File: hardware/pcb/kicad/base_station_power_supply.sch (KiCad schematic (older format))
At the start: 18 parts, among them CON1 POWER_JACK_TART, IC1 BRIDGE_TART

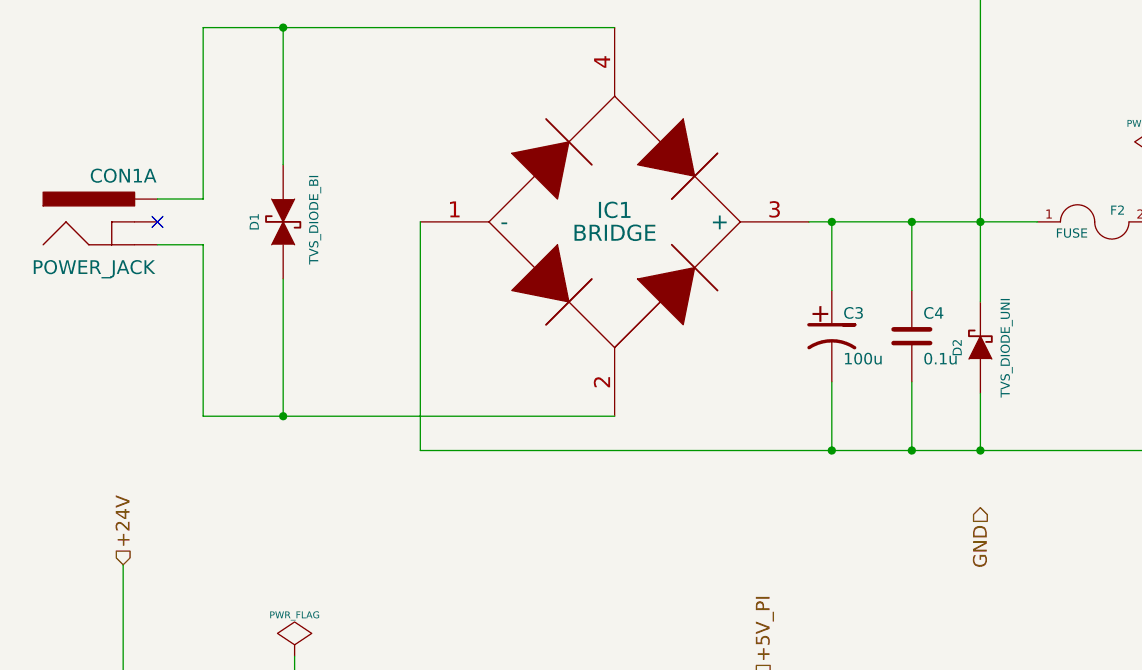
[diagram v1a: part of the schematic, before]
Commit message: New libraries, and board updates
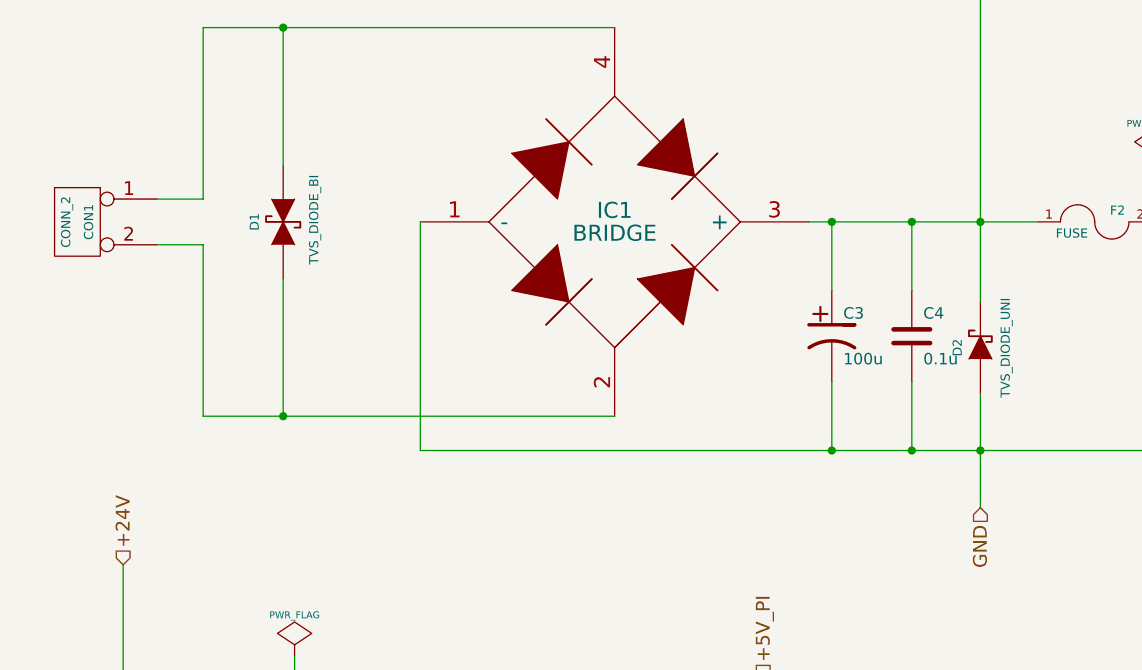
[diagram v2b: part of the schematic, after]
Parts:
- removed CON1: POWER_JACK_TART, symbol POWER_JACK_TART
- added CON1: CONN_2, symbol CONN_2
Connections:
- net GND: now also C3.2, C4.2, C5.2, C6.2, C7.2, D2.1 (A), D3.2 (K), IC1.1 (-), REG2.2 (GND), REG3.2 (GND)
- net at D1.1 (A), IC1.2: now also CON1.2 (PM)
- net at D1.2 (K), IC1.4: now also CON1.1 (P1)
- no-connect marks 1 -> 0
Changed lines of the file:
@@
 Sheet 2 7
 Title ""
-Date "26 sep 2014"
+Date "6 oct 2014"
 Rev ""
 Comp ""
@@
 	3200 6400 4650 6400
 Wire Wire Line
-	5600 4350 5600 4600
+	5600 4350 5600 4850
 Text HLabel 4650 6550 3    60   Input ~ 0
 GND
@@
 F 4 "OKI-78SR" H 6950 3854 60  0000 C CNN "NAME"
 	1    6950 3650
-	1    0    0    -1
-$EndComp
-$Comp
-L POWER_JACK_TART CON1
-U 1 1 5418E80C
-P 1600 3700
-F 0 "CON1" H 1850 4000 60  0000 C CNN
-F 1 "POWER_JACK_TART" H 1600 4110 60  0001 C CNN
-F 2 "" H 1600 3700 60  0001 C CNN
-F 3 "" H 1600 3700 60  0001 C CNN
-F 4 "POWER_JACK" H 1720 3600 60  0000 C CNN "NAME"
-	1    1600 3700
 	1    0    0    -1
 $EndComp
@@
 	1    0    0    -1
 $EndComp
-NoConn ~ 2000 3600
 Text HLabel 5600 4850 3    60   Input ~ 0
 GND
@@
 	1    0    0    -1
 $EndComp
+$Comp
+L CONN_2 CON1
+U 1 1 542A164F
+P 1650 3600
+F 0 "CON1" V 1600 3600 40  0000 C CNN
+F 1 "CONN_2" V 1700 3600 40  0000 C CNN
+F 2 "" H 1650 3600 60  0000 C CNN
+F 3 "" H 1650 3600 60  0000 C CNN
+	1    1650 3600
+	-1   0    0    -1
+$EndComp
 $EndSCHEMATC
